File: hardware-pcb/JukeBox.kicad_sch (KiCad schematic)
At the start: 91 parts, among them J1 USB4105-GF-A, Q1 Q_NPN_ECB, SW1 SW_SPST, SW10 SW_SPST, SW11 SW_SPST, SW12 SW_SPST, SW2 SW_SPST, SW3 SW_SPST, SW4 SW_SPST, SW5 SW_SPST, SW6 SW_SPST, SW7 SW_SPST, SW8 SW_SPST, SW9 SW_SPST, U1 NCP1117-3.3_SOT223, U2 W25Q128JVS, U3 RP2040, U4 st7789v, Y1 ECS-120-20-33-AEL-TR

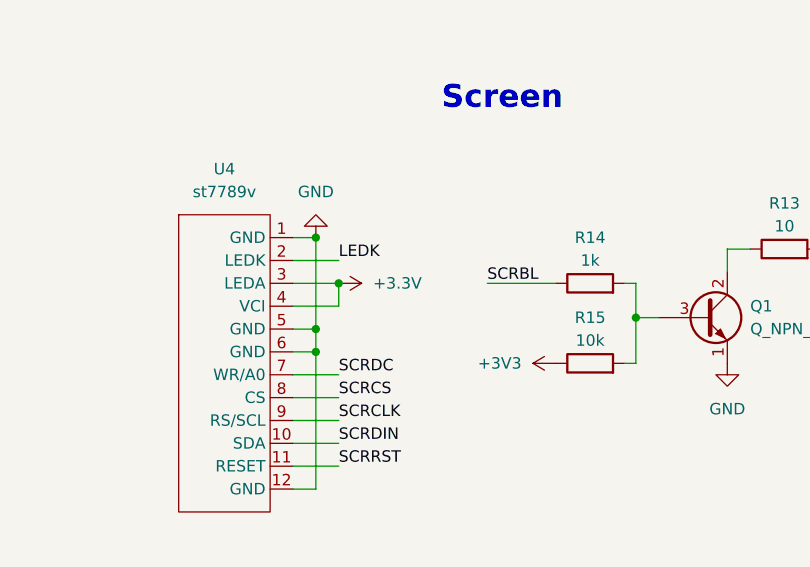
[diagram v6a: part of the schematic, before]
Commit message: rearrange board, new 100x100mm design
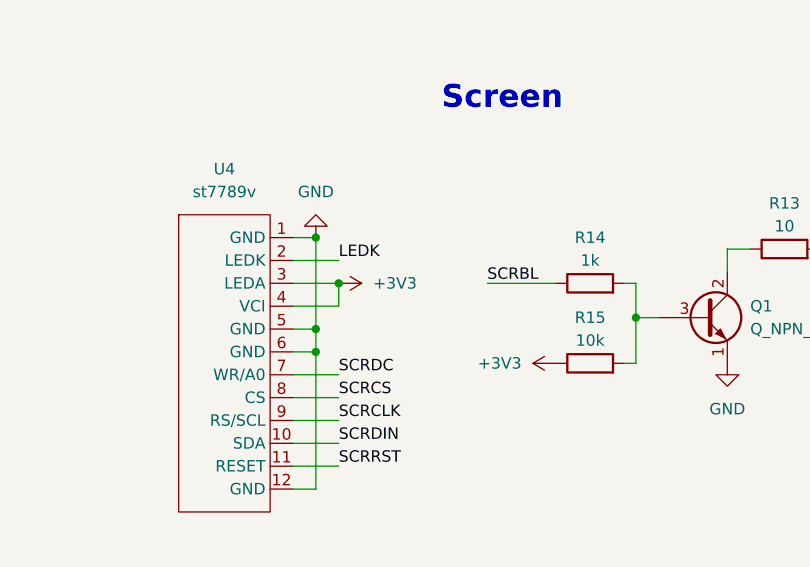
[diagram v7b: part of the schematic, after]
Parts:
- TP1, TP11, TP12, TP13, TP14, TP2, TP21, TP22, TP23, TP24, TP25, TP26, TP27, TP31, TP32, TP33, TP34, TP35, TP36, TP41, TP42: footprint TestPoint:TestPoint_Pad_D4.0mm -> TestPoint:TestPoint_Pad_D1.0mm
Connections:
- net +3.3V is gone; now on net +3V3: U4.3 (LEDA), U4.4 (VCI)
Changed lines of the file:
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@@
 	)
 	(junction
+		(at 209.55 177.8)
+		(diameter 0)
+		(color 0 0 0 0)
+	)
+	(junction
 		(at 374.65 19.05)
 		(diameter 0)
@@
 		(color 0 0 0 0)
 	)
-	(junction
-		(at 209.55 177.8)
-		(diameter 0)
-		(color 0 0 0 0)
-	)
 	(no_connect
 		(at 29.21 46.99)
@@
 			)
 		)
-		(property "Footprint" "TestPoint:TestPoint_Pad_D4.0mm"
+		(property "Footprint" "TestPoint:TestPoint_Pad_D1.0mm"
 			(at 193.04 270.51 0)
 			(effects
@@
 			)
 		)
-		(property "Footprint" "TestPoint:TestPoint_Pad_D4.0mm"
+		(property "Footprint" "TestPoint:TestPoint_Pad_D1.0mm"
 			(at 193.04 260.35 0)
 			(effects
@@
 			)
 		)
-		(property "Footprint" "TestPoint:TestPoint_Pad_D4.0mm"
+		(property "Footprint" "TestPoint:TestPoint_Pad_D1.0mm"
 			(at 193.04 273.05 0)
 			(effects
@@
 	)
 	(symbol
+		(lib_id "power:+3V3")
+		(at 209.55 177.8 270)
+		(unit 1)
+		(exclude_from_sim no)
+		(in_bom yes)
+		(on_board yes)
+		(dnp no)
+		(fields_autoplaced yes)
+		(property "Reference" "#PWR01"
+			(at 205.74 177.8 0)
+			(effects
+				(font
+					(size 1.27 1.27)
+				)
+				(hide yes)
+			)
+		)
+		(property "Value" "+3V3"
+			(at 213.36 177.7999 90)
+			(effects
+				(font
+					(size 1.27 1.27)
+				)
+				(justify left)
+			)
+		)
+		(property "Footprint" ""
+			(at 209.55 177.8 0)
+			(effects
+				(font
+					(size 1.27 1.27)
+				)
+				(hide yes)
+			)
+		)
+		(property "Datasheet" ""
+			(at 209.55 177.8 0)
+			(effects
+				(font
+					(size 1.27 1.27)
+				)
+				(hide yes)
+			)
+		)
+		(property "Description" ""
+			(at 209.55 177.8 0)
+			(effects
+				(font
+					(size 1.27 1.27)
+				)
+				(hide yes)
+			)
+		)
+		(pin "1"
+		)
+		(instances
+			(project "JukeBox"
+				(path "/6328db6d-b3ae-4344-8bbe-195d6ec45eb3"
+					(reference "#PWR01")
+					(unit 1)
+				)
+			)
+		)
+	)
+	(symbol
 		(lib_id "Simulation_SPICE:DIODE")
 		(at 346.71 218.44 180)
@@
 			)
 		)
-		(property "Footprint" "TestPoint:TestPoint_Pad_D4.0mm"
+		(property "Footprint" "TestPoint:TestPoint_Pad_D1.0mm"
 			(at 222.25 260.35 0)
 			(effects
@@
 			)
 		)
-		(property "Footprint" "TestPoint:TestPoint_Pad_D4.0mm"
+		(property "Footprint" "TestPoint:TestPoint_Pad_D1.0mm"
 			(at 222.25 255.27 0)
 			(effects
@@
 			)
 		)
-		(property "Footprint" "TestPoint:TestPoint_Pad_D4.0mm"
+		(property "Footprint" "TestPoint:TestPoint_Pad_D1.0mm"
 			(at 222.25 262.89 0)
 			(effects
@@
 			)
 		)
-		(property "Footprint" "TestPoint:TestPoint_Pad_D4.0mm"
+		(property "Footprint" "TestPoint:TestPoint_Pad_D1.0mm"
 			(at 222.25 267.97 0)
 			(effects
@@
 			)
 		)
-		(property "Footprint" "TestPoint:TestPoint_Pad_D4.0mm"
+		(property "Footprint" "TestPoint:TestPoint_Pad_D1.0mm"
 			(at 193.04 267.97 0)
 			(effects
@@
 			)
 		)
-		(property "Footprint" "TestPoint:TestPoint_Pad_D4.0mm"
+		(property "Footprint" "TestPoint:TestPoint_Pad_D1.0mm"
 			(at 222.25 257.81 0)
 			(effects
@@
 	)
 	(symbol
-		(lib_id "power:+3.3V")
-		(at 209.55 177.8 270)
-		(unit 1)
-		(exclude_from_sim no)
-		(in_bom yes)
-		(on_board yes)
-		(dnp no)
-		(fields_autoplaced yes)
-		(property "Reference" "#PWR0115"
-			(at 205.74 177.8 0)
-			(effects
-				(font
-					(size 1.27 1.27)
-				)
-				(hide yes)
-			)
-		)
-		(property "Value" "+3.3V"
-			(at 213.36 177.7999 90)
-			(effects
-				(font
-					(size 1.27 1.27)
-				)
-				(justify left)
-			)
-		)
-		(property "Footprint" ""
-			(at 209.55 177.8 0)
-			(effects
-				(font
-					(size 1.27 1.27)
-				)
-				(hide yes)
-			)
-		)
-		(property "Datasheet" ""
-			(at 209.55 177.8 0)
-			(effects
-				(font
-					(size 1.27 1.27)
-				)
-				(hide yes)
-			)
-		)
-		(property "Description" ""
-			(at 209.55 177.8 0)
-			(effects
-				(font
-					(size 1.27 1.27)
-				)
-				(hide yes)
-			)
-		)
-		(pin "1"
-		)
-		(instances
-			(project ""
-				(path "/6328db6d-b3ae-4344-8bbe-195d6ec45eb3"
-					(reference "#PWR0115")
-					(unit 1)
-				)
-			)
-		)
-	)
-	(symbol
 		(lib_id "power:GND")
 		(at 381 200.66 180)
@@
 			)
 		)
-		(property "Footprint" "TestPoint:TestPoint_Pad_D4.0mm"
+		(property "Footprint" "TestPoint:TestPoint_Pad_D1.0mm"
 			(at 193.04 265.43 0)
 			(effects
@@
 			)
 		)
-		(property "Footprint" "TestPoint:TestPoint_Pad_D4.0mm"
+		(property "Footprint" "TestPoint:TestPoint_Pad_D1.0mm"
 			(at 222.25 265.43 0)
 			(effects
@@
 			)
 		)
-		(property "Footprint" "TestPoint:TestPoint_Pad_D4.0mm"
+		(property "Footprint" "TestPoint:TestPoint_Pad_D1.0mm"
 			(at 165.1 265.43 0)
 			(effects
@@
 			)
 		)
-		(property "Footprint" "TestPoint:TestPoint_Pad_D4.0mm"
+		(property "Footprint" "TestPoint:TestPoint_Pad_D1.0mm"
 			(at 193.04 257.81 0)
 			(effects
@@
 			)
 		)
-		(property "Footprint" "TestPoint:TestPoint_Pad_D4.0mm"
+		(property "Footprint" "TestPoint:TestPoint_Pad_D1.0mm"
 			(at 165.1 256.54 0)
 			(effects
@@
 			)
 		)
-		(property "Footprint" "TestPoint:TestPoint_Pad_D4.0mm"
+		(property "Footprint" "TestPoint:TestPoint_Pad_D1.0mm"
 			(at 222.25 273.05 0)
 			(effects
@@
 			)
 		)
-		(property "Footprint" "TestPoint:TestPoint_Pad_D4.0mm"
+		(property "Footprint" "TestPoint:TestPoint_Pad_D1.0mm"
 			(at 222.25 275.59 0)
 			(effects
@@
 			)
 		)
-		(property "Footprint" "TestPoint:TestPoint_Pad_D4.0mm"
+		(property "Footprint" "TestPoint:TestPoint_Pad_D1.0mm"
 			(at 165.1 259.08 0)
 			(effects
@@
 			)
 		)
-		(property "Footprint" "TestPoint:TestPoint_Pad_D4.0mm"
+		(property "Footprint" "TestPoint:TestPoint_Pad_D1.0mm"
 			(at 165.1 270.51 0)
 			(effects
@@
 			)
 		)
-		(property "Footprint" "TestPoint:TestPoint_Pad_D4.0mm"
+		(property "Footprint" "TestPoint:TestPoint_Pad_D1.0mm"
 			(at 165.1 267.97 0)
 			(effects
@@
 			)
 		)
-		(property "Footprint" "TestPoint:TestPoint_Pad_D4.0mm"
+		(property "Footprint" "TestPoint:TestPoint_Pad_D1.0mm"
 			(at 165.1 273.05 0)
 			(effects
@@
 			)
 		)
-		(property "Footprint" "TestPoint:TestPoint_Pad_D4.0mm"
+		(property "Footprint" "TestPoint:TestPoint_Pad_D1.0mm"
 			(at 193.04 255.27 0)
 			(effects

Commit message: change mounting to via pads
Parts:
- H1, H2, H3, H4: footprint MountingHole:MountingHole_3.2mm_M3 -> MountingHole:MountingHole_3.2mm_M3_Pad_Via
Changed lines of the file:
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@@
 			)
 		)
-		(property "Footprint" "MountingHole:MountingHole_3.2mm_M3"
+		(property "Footprint" "MountingHole:MountingHole_3.2mm_M3_Pad_Via"
 			(at 279.4 264.16 0)
 			(effects
@@
 			)
 		)
-		(property "Footprint" "MountingHole:MountingHole_3.2mm_M3"
+		(property "Footprint" "MountingHole:MountingHole_3.2mm_M3_Pad_Via"
 			(at 279.4 269.24 0)
 			(effects
@@
 			)
 		)
-		(property "Footprint" "MountingHole:MountingHole_3.2mm_M3"
+		(property "Footprint" "MountingHole:MountingHole_3.2mm_M3_Pad_Via"
 			(at 279.4 274.32 0)
 			(effects
@@
 			)
 		)
-		(property "Footprint" "MountingHole:MountingHole_3.2mm_M3"
+		(property "Footprint" "MountingHole:MountingHole_3.2mm_M3_Pad_Via"
 			(at 279.4 279.4 0)
 			(effects
